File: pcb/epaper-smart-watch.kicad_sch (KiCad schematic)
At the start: 67 parts, among them J1 AXT624124, J3 Lithium Battery 3.7V, M1 Motor_DC, P1 USB_C_Plug_USB2.0, Q1 MMBT3904, Q3 Si1308EDL, SW1 BTN, SW2 BTN, SW3 BTN, SW4 BTN, U1 CH340E, U2 STM32WB1MMCH6TR, U3 LSM6DSOWTR

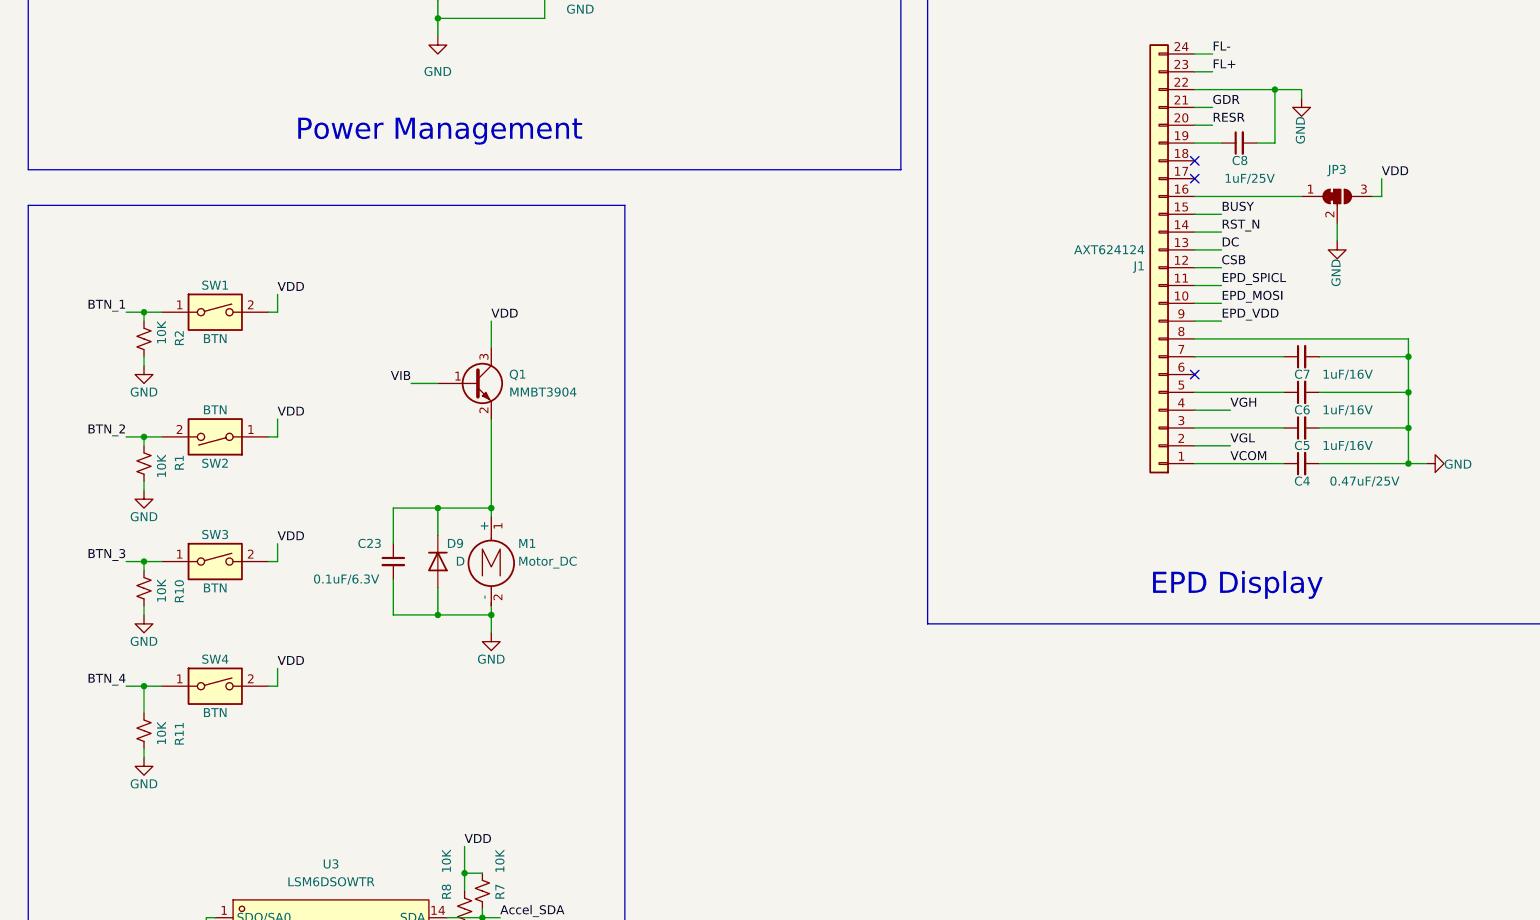
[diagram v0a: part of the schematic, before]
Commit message: Thickened power traces, fixed JP3 and removed pulldowns for buttons
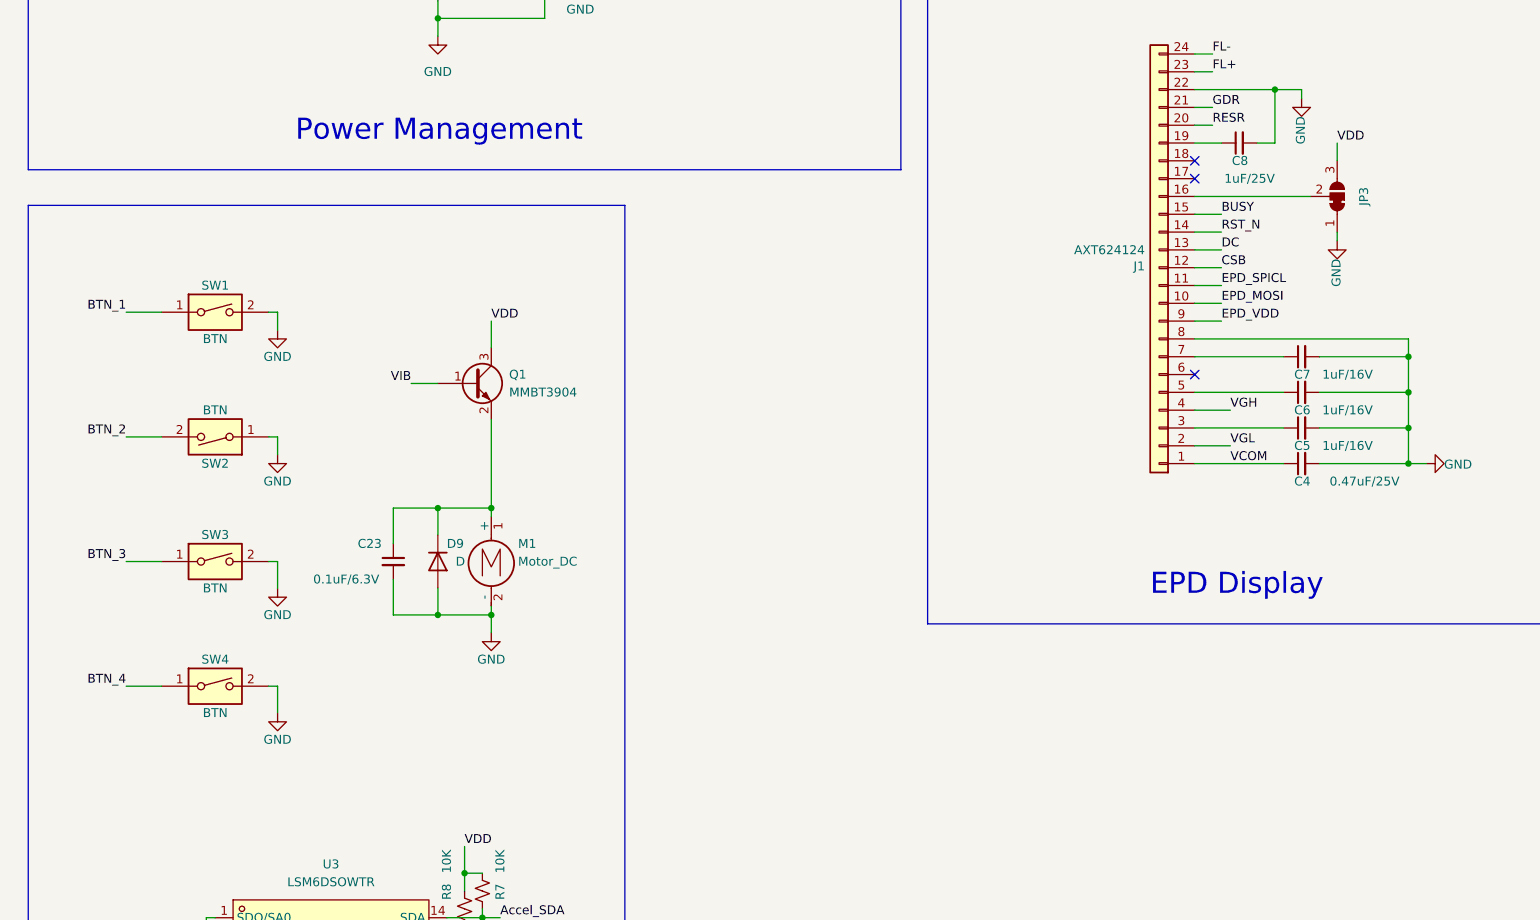
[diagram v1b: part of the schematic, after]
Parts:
- removed R1, R10, R11, R2: 10K, Resistor_SMD:R_0402_1005Metric, symbol Device:R_Small_US
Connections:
- net EPD_VDD: no longer SW1.2, SW2.1, SW3.2, SW4.2
- net GND: now also JP3.1 (A), SW1.2, SW2.1, SW3.2, SW4.2; no longer JP3.2 (C)
- net at J1.16 (Pin_16): now also JP3.2 (C); no longer JP3.1 (A)
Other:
- moved on the sheet: JP3
